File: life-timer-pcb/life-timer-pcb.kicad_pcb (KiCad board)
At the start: 2 copper layers, 39 x 31.8 mm, 16 parts, among them J1 SSD1306_Socket, SW1 SW_RST, SW2 BTN0, SW3 BTN1, SW4 BTN2, SW5 SW_PWR, U1 ATtiny85-20S

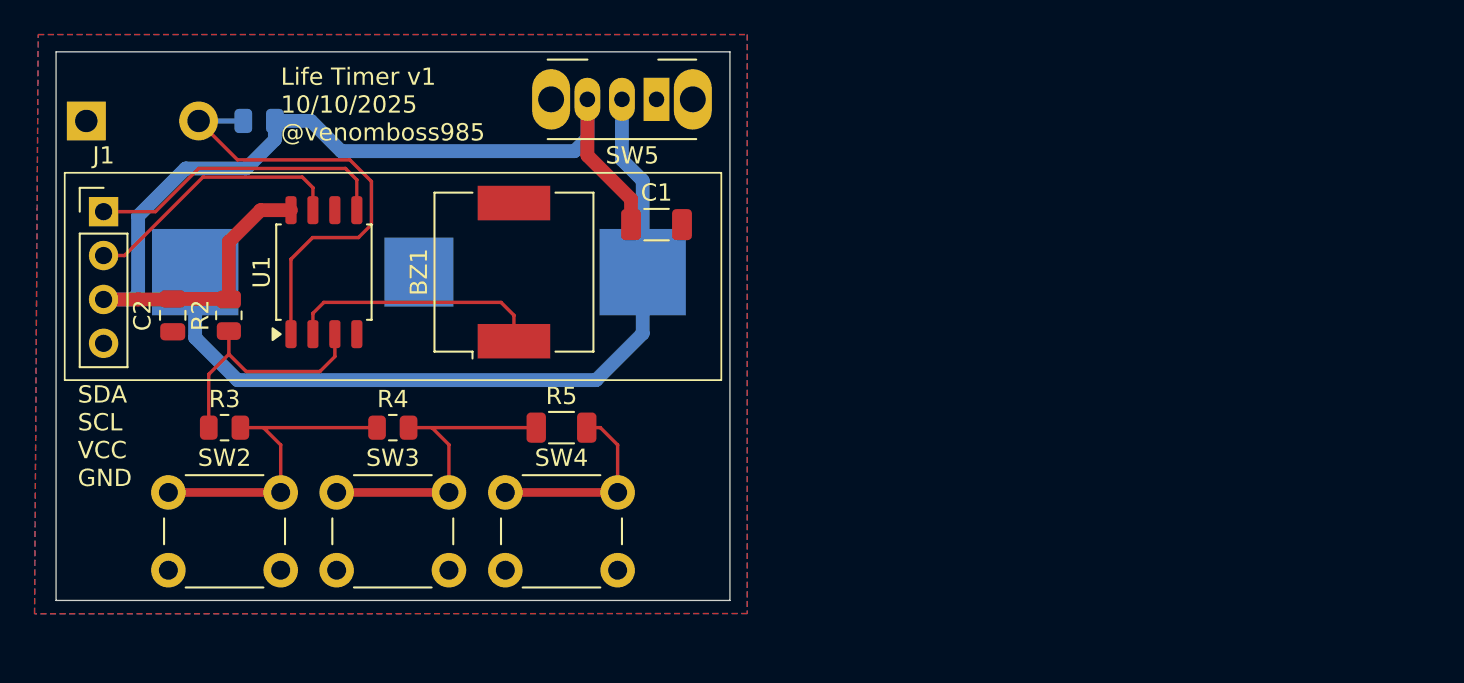
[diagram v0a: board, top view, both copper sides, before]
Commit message: Updated page settings for schematic and PCB
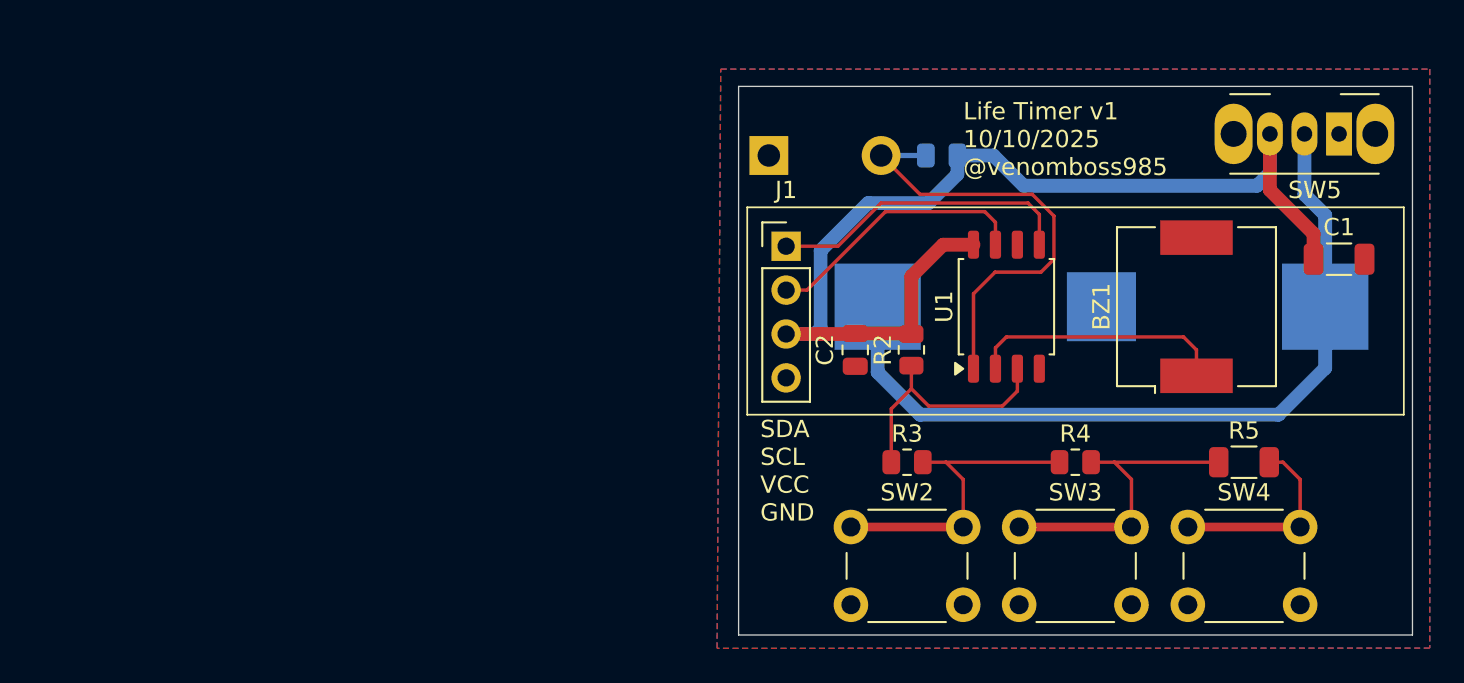
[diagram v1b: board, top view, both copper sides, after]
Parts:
- moved R4 39.6 mm to (146.5, 107.8)
- moved SW3 39.6 mm to (143.2, 111.5)
- moved BT1 39.6 mm to (148.0, 98.8)
- moved BZ1 39.6 mm to (153.5, 98.8)
- moved C1 39.6 mm to (161.8, 96.0)
- moved C2 39.6 mm to (133.8, 101.2)
- moved J1 39.6 mm to (129.8, 95.2)
- moved R1 39.6 mm to (138.8, 90.0)
- moved R2 39.6 mm to (137.0, 101.2)
- moved R3 39.6 mm to (136.8, 107.8)
- moved R5 39.6 mm to (156.2, 107.8)
- moved SW1 39.6 mm to (128.8, 90.0)
- moved SW2 39.6 mm to (133.5, 111.5)
- moved SW4 39.6 mm to (153.0, 111.5)
- moved SW5 39.6 mm to (161.8, 88.8)
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
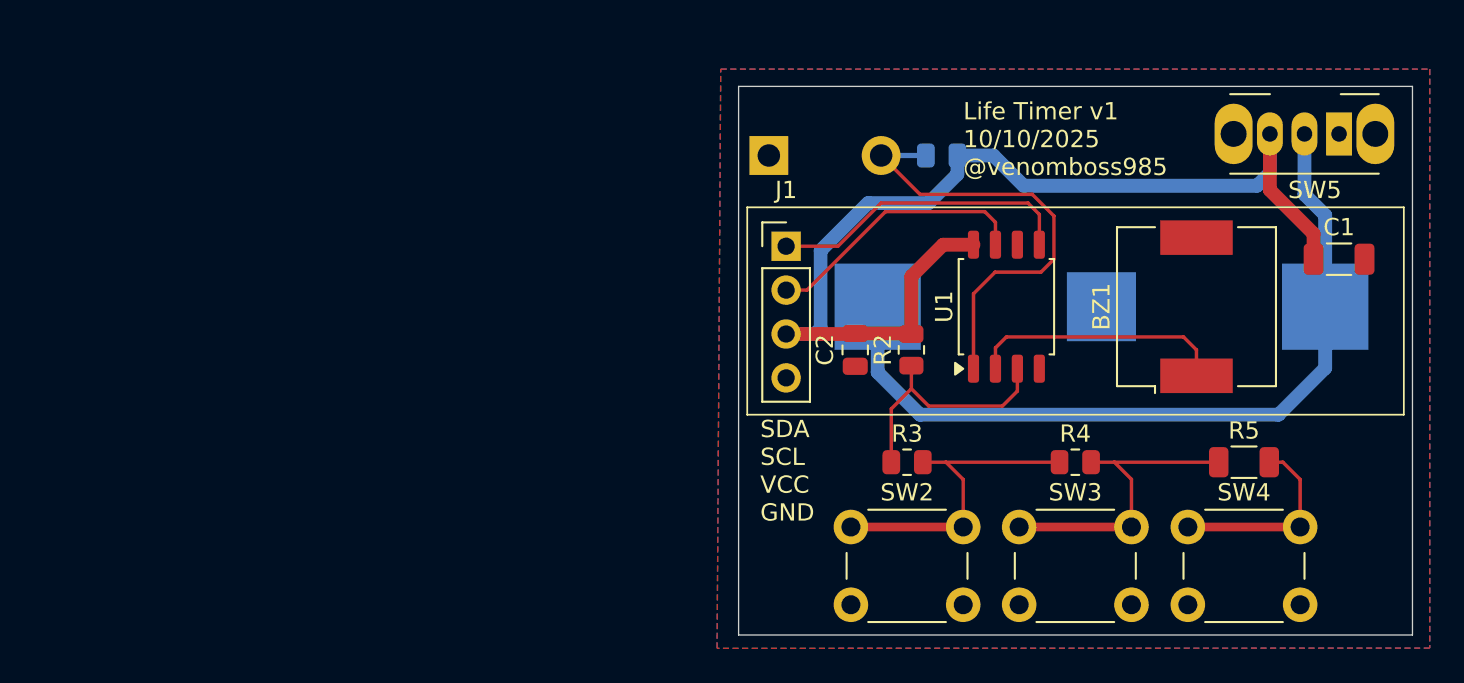
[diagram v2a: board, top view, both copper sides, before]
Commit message: Adjusted layout to be slightly shorter with mounting holes
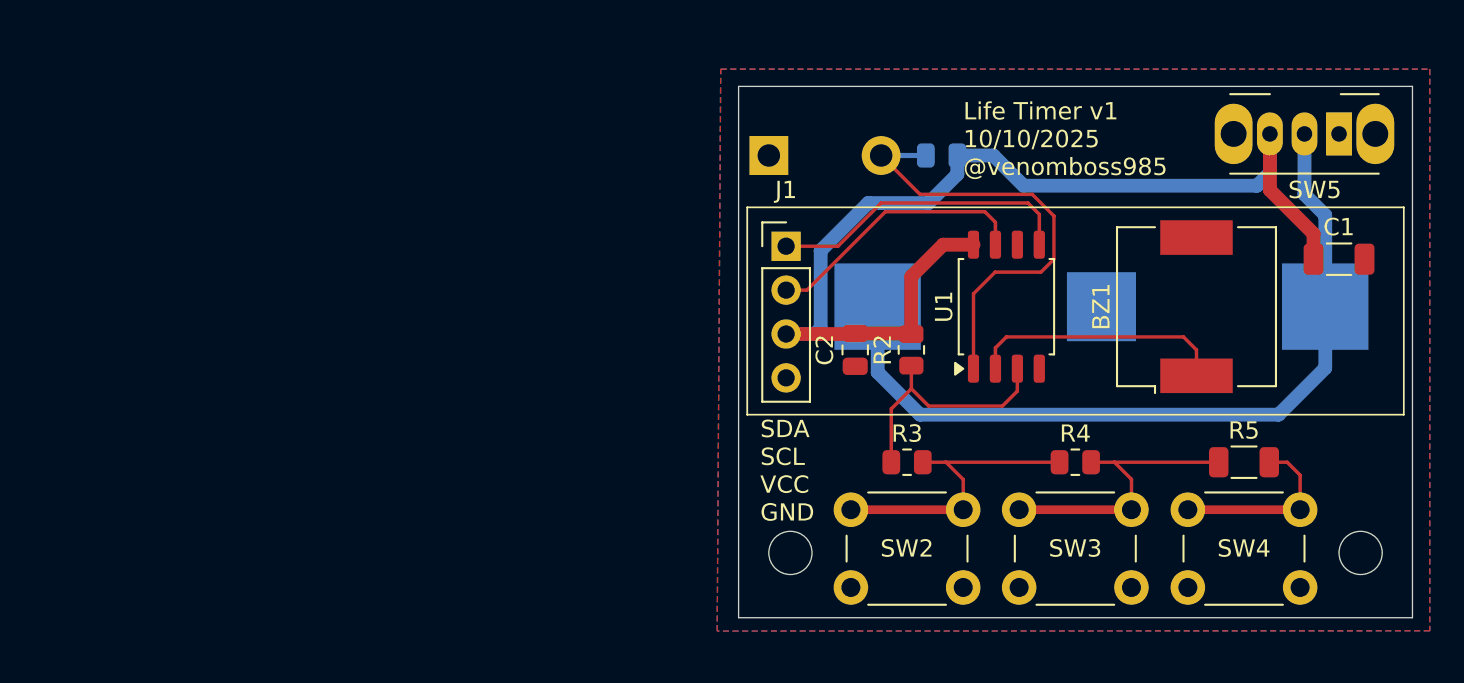
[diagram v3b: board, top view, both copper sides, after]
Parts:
- moved SW2 1.00 mm to (133.5, 110.5)
- moved SW3 1.00 mm to (143.2, 110.5)
- moved SW4 1.00 mm to (153.0, 110.5)
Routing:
- net Net-(R4-Pad2): track 18.0 -> 17.0 mm
- net Net-(R3-Pad2): track 18.6 -> 17.6 mm
- net Net-(R5-Pad2): track 11.5 -> 10.6 mm
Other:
- board size 39 x 31.8 mm -> 39 x 30.8 mm

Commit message: Filleted corners and adjusted silkscreen and reset switch slightly
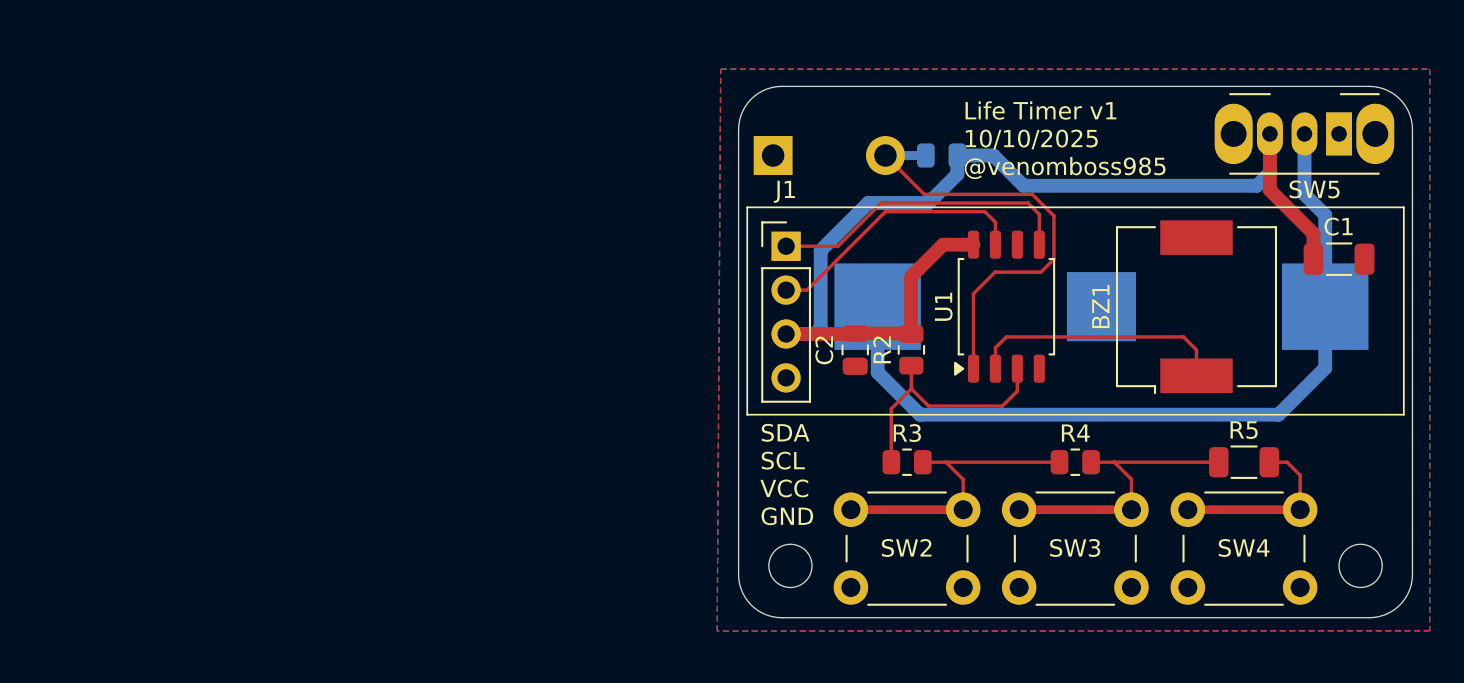
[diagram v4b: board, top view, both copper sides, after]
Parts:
- moved SW1 0.25 mm to (129.0, 90.0)
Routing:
- net ~{RESET}: track 26.4 -> 25.9 mm
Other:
- outline, holes or cut-outs redrawn
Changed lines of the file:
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@@
 	(footprint "Button_Switch_THT:SW_PUSH_1P1T_6x3.5mm_H4.3_APEM_MJTP1243"
 		(layer "B.Cu")
-		(at 128.75 90)
+		(at 129 90)
 		(descr "tactile push button, 6x3.5mm, https://www.apem.com/idec-apem/en_US/PCB-switches/Tactile-Switches/MJTP-6mm-through-hole/c/MJTP_6mm_through%20hole?page=1")
 		(tags "PHAP3362 6mm tact sw THT")
@@
 		(layer "F.SilkS")
 	)
-	(gr_rect
-		(start 127 86)
-		(end 166 116.75)
+	(gr_line
+		(start 163.5 116.75)
+		(end 129.5 116.75)
 		(stroke
 			(width 0.05)
 			(type default)
 		)
-		(fill no)
 		(layer "Edge.Cuts")
 	)
+	(gr_arc
+		(start 166 114.25)
+		(mid 165.267767 116.017767)
+		(end 163.5 116.75)
+		(stroke
+			(width 0.05)
+			(type default)
+		)
+		(layer "Edge.Cuts")
+	)
+	(gr_arc
+		(start 163.5 86)
+		(mid 165.267767 86.732233)
+		(end 166 88.5)
+		(stroke
+			(width 0.05)
+			(type default)
+		)
+		(layer "Edge.Cuts")
+	)
+	(gr_line
+		(start 127 114.25)
+		(end 127 88.5)
+		(stroke
+			(width 0.05)
+			(type default)
+		)
+		(layer "Edge.Cuts")
+	)
+	(gr_line
+		(start 129.5 86)
+		(end 163.5 86)
+		(stroke
+			(width 0.05)
+			(type default)
+		)
+		(layer "Edge.Cuts")
+	)
+	(gr_line
+		(start 166 88.5)
+		(end 166 114.25)
+		(stroke
+			(width 0.05)
+			(type default)
+		)
+		(layer "Edge.Cuts")
+	)
+	(gr_arc
+		(start 127 88.5)
+		(mid 127.732233 86.732233)
+		(end 129.5 86)
+		(stroke
+			(width 0.05)
+			(type default)
+		)
+		(layer "Edge.Cuts")
+	)
+	(gr_arc
+		(start 129.5 116.75)
+		(mid 127.732233 116.017767)
+		(end 127 114.25)
+		(stroke
+			(width 0.05)
+			(type default)
+		)
+		(layer "Edge.Cuts")
+	)
 	(gr_circle
-		(center 163 113)
-		(end 164.25 113)
+		(center 163 113.75)
+		(end 164.25 113.75)
 		(stroke
 			(width 0.05)
@@
 	)
 	(gr_circle
-		(center 130 113)
-		(end 131.25 113)
+		(center 130 113.75)
+		(end 131.25 113.75)
 		(stroke
 			(width 0.05)
@@
 	)
 	(gr_text "SDA\nSCL\nVCC\nGND"
-		(at 128.25 111.25 0)
+		(at 128.25 111.5 0)
 		(layer "F.SilkS")
 		(effects
@@
 	)
 	(gr_text "CR2032"
-		(at 150.75 108.75 0)
+		(at 150.75 108 0)
 		(layer "B.SilkS")
 		(effects
@@
 	)
 	(segment
+		(start 137.75 92.25)
+		(end 135.5 90)
+		(width 0.2)
+		(layer "F.Cu")
+		(net 6)
+	)
+	(segment
+		(start 144.5 96.75)
+		(end 145.25 96)
+		(width 0.2)
+		(layer "F.Cu")
+		(net 6)
+	)
+	(segment
+		(start 144 92.25)
+		(end 137.75 92.25)
+		(width 0.2)
+		(layer "F.Cu")
+		(net 6)
+	)
+	(segment
+		(start 140.595 98)
+		(end 141.845 96.75)
+		(width 0.2)
+		(layer "F.Cu")
+		(net 6)
+	)
+	(segment
+		(start 145.25 96)
+		(end 145.25 93.5)
+		(width 0.2)
+		(layer "F.Cu")
+		(net 6)
+	)
+	(segment
+		(start 145.25 93.5)
+		(end 144 92.25)
+		(width 0.2)
+		(layer "F.Cu")
+		(net 6)
+	)
+	(segment
+		(start 140.595 102.3375)
+		(end 140.595 98)
+		(width 0.2)
+		(layer "F.Cu")
+		(net 6)
+	)
+	(segment
 		(start 141.845 96.75)
-		(end 140.595 98)
+		(end 144.5 96.75)
 		(width 0.2)
 		(layer "F.Cu")
@@
 	)
 	(segment
-		(start 145.25 96)
-		(end 144.5 96.75)
-		(width 0.2)
-		(layer "F.Cu")
-		(net 6)
-	)
-	(segment
-		(start 145.25 93.5)
-		(end 145.25 96)
-		(width 0.2)
-		(layer "F.Cu")
-		(net 6)
-	)
-	(segment
-		(start 144 92.25)
-		(end 145.25 93.5)
-		(width 0.2)
-		(layer "F.Cu")
-		(net 6)
-	)
-	(segment
-		(start 144.5 96.75)
-		(end 141.845 96.75)
-		(width 0.2)
-		(layer "F.Cu")
-		(net 6)
-	)
-	(segment
-		(start 140.595 98)
-		(end 140.595 102.3375)
-		(width 0.2)
-		(layer "F.Cu")
-		(net 6)
-	)
-	(segment
-		(start 135.25 90)
-		(end 137.5 92.25)
-		(width 0.2)
-		(layer "F.Cu")
-		(net 6)
-	)
-	(segment
-		(start 137.5 92.25)
-		(end 144 92.25)
-		(width 0.2)
-		(layer "F.Cu")
-		(net 6)
-	)
-	(segment
-		(start 135.25 90)
-		(end 137.8375 90)
-		(width 0.3)
+		(start 137.8375 90)
+		(end 135.5 90)
+		(width 0.5)
 		(layer "B.Cu")
 		(net 6)

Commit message: Fixed input buttons to show up as the same part on the BOM
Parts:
- SW2: value BTN0 -> SW_Push
- SW3: value BTN1 -> SW_Push
- SW4: value BTN2 -> SW_Push
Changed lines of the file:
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@@
 			)
 		)
-		(property "Value" "BTN1"
+		(property "Value" "SW_Push"
 			(at 3.75 6.7 0)
 			(layer "F.Fab")
@@
 			)
 		)
-		(property "Value" "BTN2"
+		(property "Value" "SW_Push"
 			(at 3.75 6.7 0)
 			(layer "F.Fab")
@@
 			)
 		)
-		(property "Value" "BTN0"
+		(property "Value" "SW_Push"
 			(at 3.75 6.7 0)
 			(layer "F.Fab")

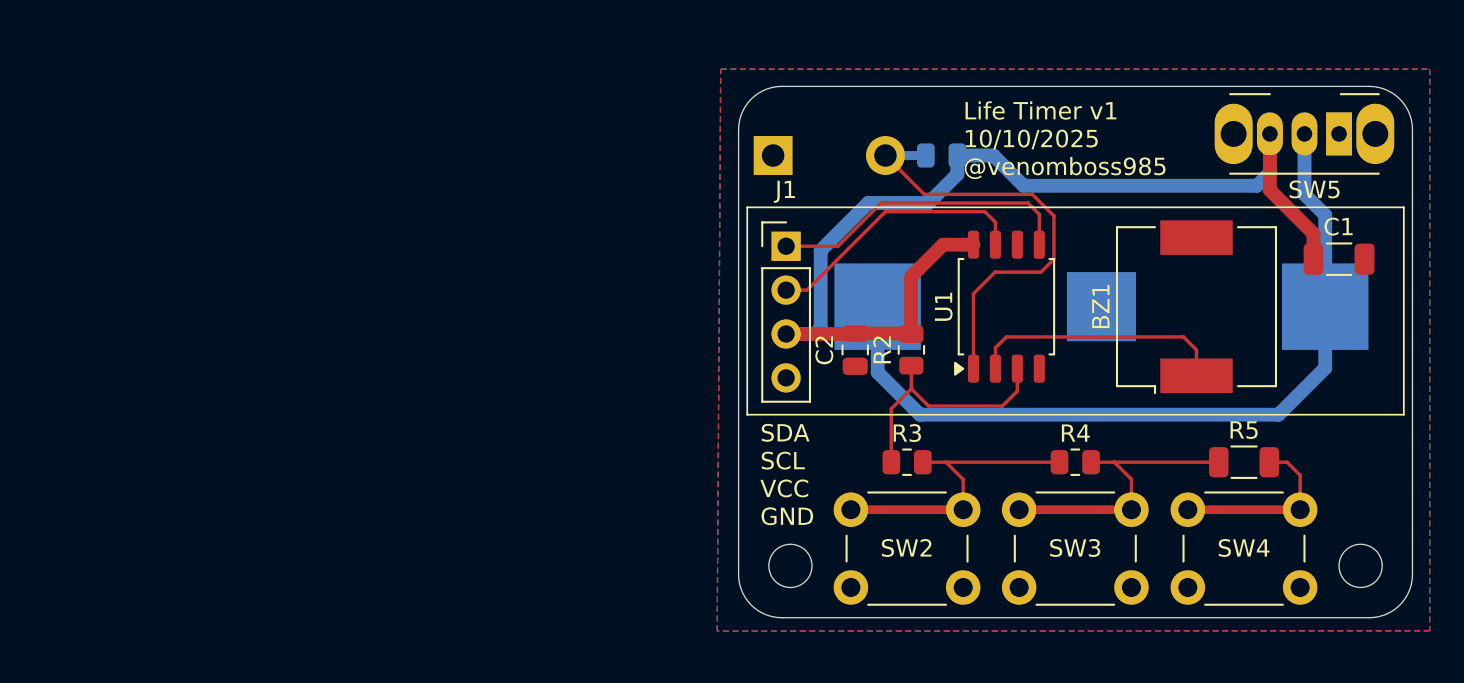
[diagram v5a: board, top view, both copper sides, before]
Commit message: Added debug LED (D1), might want to move due to spacing (place resistor between U1 and BZ1 and go from there); passes ERC/DRC
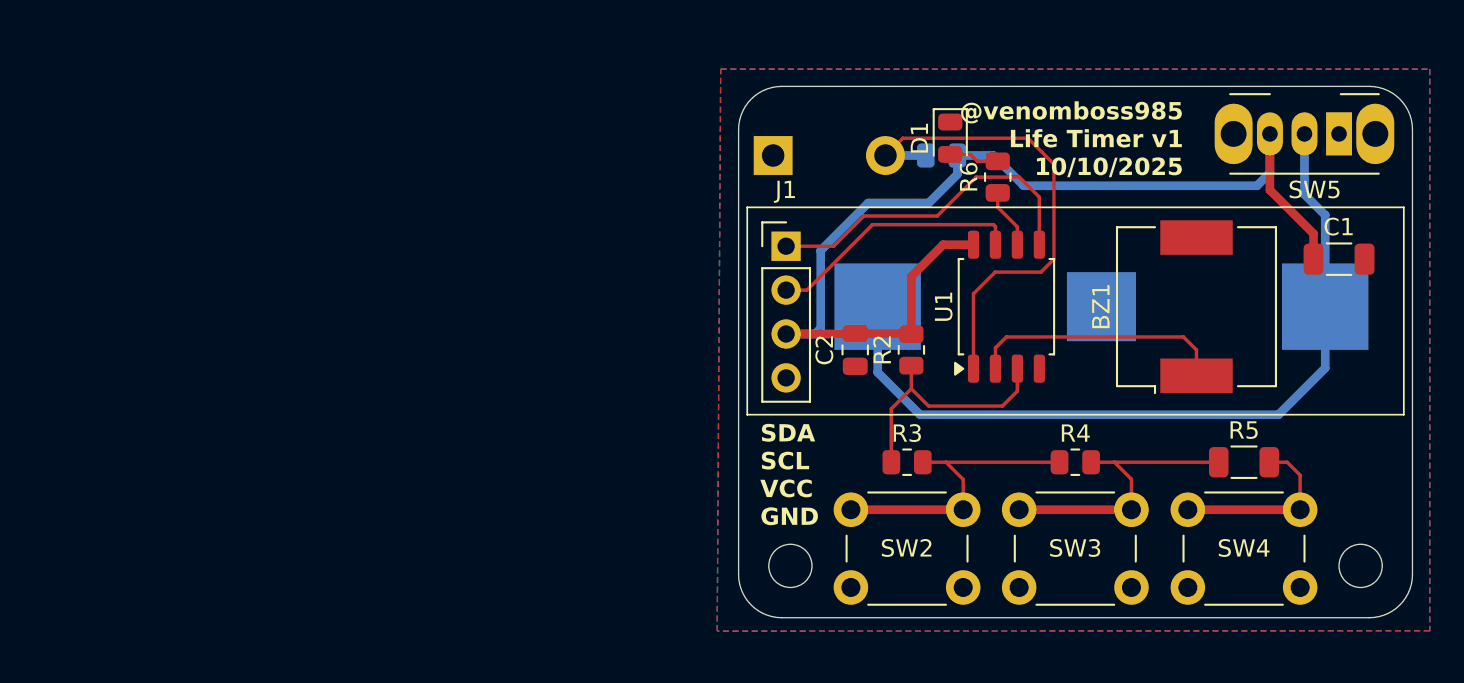
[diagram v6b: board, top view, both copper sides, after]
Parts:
- added D1: GRN, LED_SMD:LED_0805_2012Metric, F.Cu at (139.2, 89.0)
- added R6: 680, Resistor_SMD:R_0805_2012Metric, F.Cu at (142.0, 91.2)
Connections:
- U1 pad 6: unconnected-(U1-PB1-Pad6) -> Net-(U1-PB1)
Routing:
- net Net-(U1-PB1): track 0.00 -> 3.47 mm
- net Net-(D1-A): track 0.00 -> 2.92 mm
- net ~{RESET}: track 25.9 -> 28.4 mm
- net SDA: track 17.7 -> 19.5 mm
- net SCL: track 15.5 -> 14.8 mm
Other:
- board text added: "@venomboss985 Life Timer v1 10/10/2025"
- board text removed: "Life Timer v1 10/10/2025 @venomboss985"
